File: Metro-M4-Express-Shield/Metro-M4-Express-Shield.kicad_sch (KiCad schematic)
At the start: 20 parts, among them SW1 SW_Push, SW2 SW_Push, SW3 SW_Push, U2 ESP32-WROOM-32E

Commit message: add schematics, update metro shield
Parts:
- removed A1: Arduino_Uno_R3_Shield, PCM_arduino-library:Arduino_Uno_R3_Shield, symbol PCM_arduino-library:Arduino_Uno_R3_Shield
- added J1: Conn_01x10, Connector_PinHeader_2.54mm:PinHeader_1x10_P2.54mm_Vertical, symbol Connector_Generic:Conn_01x10
- added J2, J4: Conn_01x08, Connector_PinHeader_2.54mm:PinHeader_1x08_P2.54mm_Vertical, symbol Connector_Generic:Conn_01x08
- added J3: Conn_01x06, Connector_PinHeader_2.54mm:PinHeader_1x06_P2.54mm_Vertical, symbol Connector_Generic:Conn_01x06
- added J5: AVR-ISP-6, Connector_PinSocket_2.54mm:PinSocket_2x03_P2.54mm_Vertical, symbol Connector:AVR-ISP-6
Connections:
- net +3.3V: now also J4.4 (Pin_4)
- net +5V_METRO: now also J4.5 (Pin_5), J5.2 (VCC)
- net A0: now also J3.1 (Pin_1)
- net A1: now also J3.2 (Pin_2)
- net A2: now also J3.3 (Pin_3)
- net A3: now also J3.4 (Pin_4)
- net A4: now also J3.5 (Pin_5)
- net A5: now also J3.6 (Pin_6)
- net AREF: now also J1.3 (Pin_3)
- net D10: now also J1.8 (Pin_8)
- net D11: now also J1.7 (Pin_7)
- net D12: now also J1.6 (Pin_6)
- net D13: now also J1.5 (Pin_5)
- net D2: now also J2.6 (Pin_6)
- net D3: now also J2.5 (Pin_5)
- net D4: now also J2.4 (Pin_4)
- net D5: now also J2.3 (Pin_3)
- net D6: now also J2.2 (Pin_2)
- net D7: now also J2.1 (Pin_1)
- net D8: now also J1.10 (Pin_10)
- net D9: now also J1.9 (Pin_9)
- net GND: now also J1.4 (Pin_4), J4.6 (Pin_6), J4.7 (Pin_7), J5.6 (GND)
- net IOREF: now also J4.2 (Pin_2)
- net MISO: now also J5.1 (MISO)
- net MOSI: now also J5.4 (MOSI)
- net SCK: now also J5.3 (SCK)
- net SCL: now also J1.1 (Pin_1)
- net SDA: now also J1.2 (Pin_2)
- net VIN: now also J4.8 (Pin_8)
- net D0 renamed D0/RX
- net D0/RX: now also J2.8 (Pin_8)
- net D1 renamed D1/TX
- net D1/TX: now also J2.7 (Pin_7)
- net SPI_RESET renamed RESET
- net RESET: now also J4.3 (Pin_3), J5.5 (~{RST})
- no-connect marks 20 -> 21
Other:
- note added: "BUTTONS"
- note added: "LEDs"
- note added: "METRO HEADERS"
- note added: "SPI"
- note added: "WiFi-module"
- moved on the sheet: C1, C2, C3, D1, D2, D3, R1, R2, R3, R4, R5, R6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

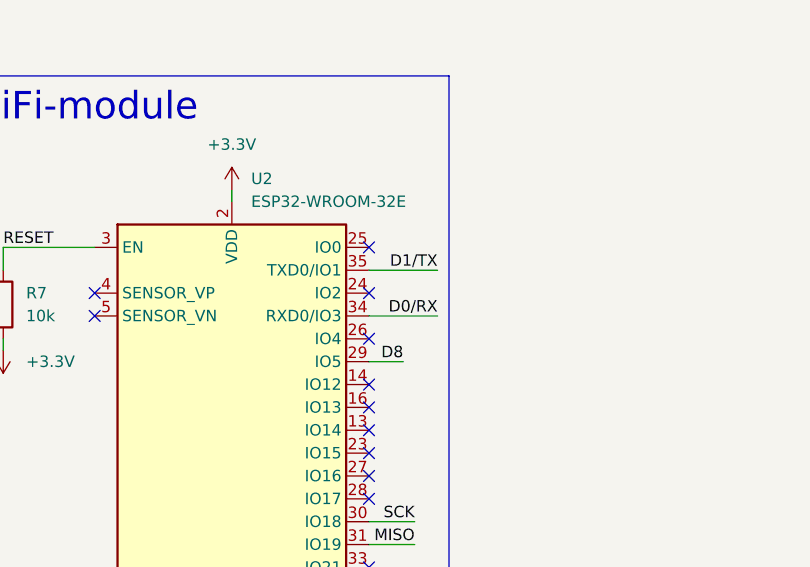
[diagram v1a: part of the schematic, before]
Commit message: fix ESP32 RX/TX connection
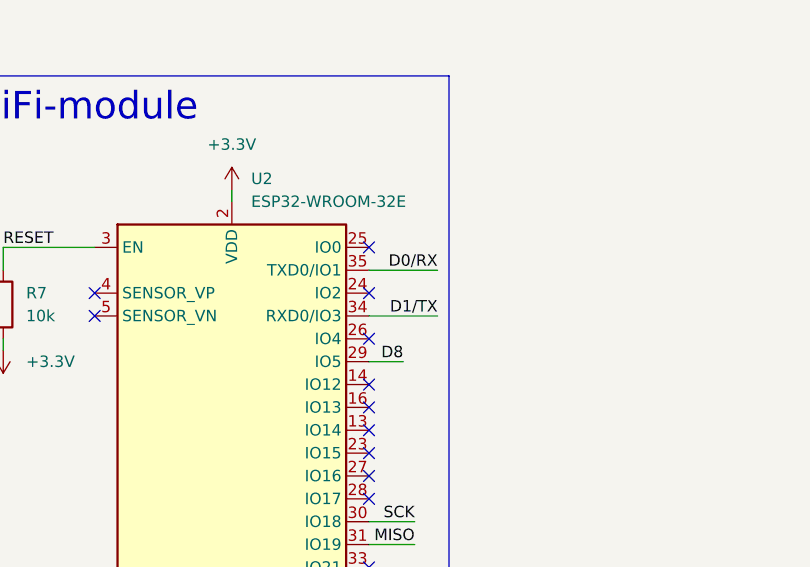
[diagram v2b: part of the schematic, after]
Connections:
- net D0/RX: now also U2.35 (TXD0/IO1); no longer U2.34 (RXD0/IO3)
- net D1/TX: now also U2.34 (RXD0/IO3); no longer U2.35 (TXD0/IO1)
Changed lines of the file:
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@@
 	)
 	(label "D1{slash}TX"
-		(at 71.12 123.19 180)
+		(at 71.12 128.27 180)
 		(effects
 			(font
@@
 	)
 	(label "D0{slash}RX"
-		(at 71.12 128.27 180)
-		(effects
-			(font
+		(at 71.12 123.19 180)
+		(effects
+			(font
